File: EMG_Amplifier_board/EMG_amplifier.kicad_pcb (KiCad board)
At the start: 2 copper layers, 50 x 28 mm, 54 parts, among them J1 Conn_01x04_Socket, J2 Conn_01x04_Pin, J3 Conn_01x06_Pin, J4 Conn_01x06_Socket, J7 Conn_01x06_Pin, U1 LPV821DBVR, U2 INA333xxDGK, U3 LPV821DBVR, U5 LPV821DBVR, U6 LPV821DBVR, U7 TPD2E001DRLR, U8 TLV8542DR

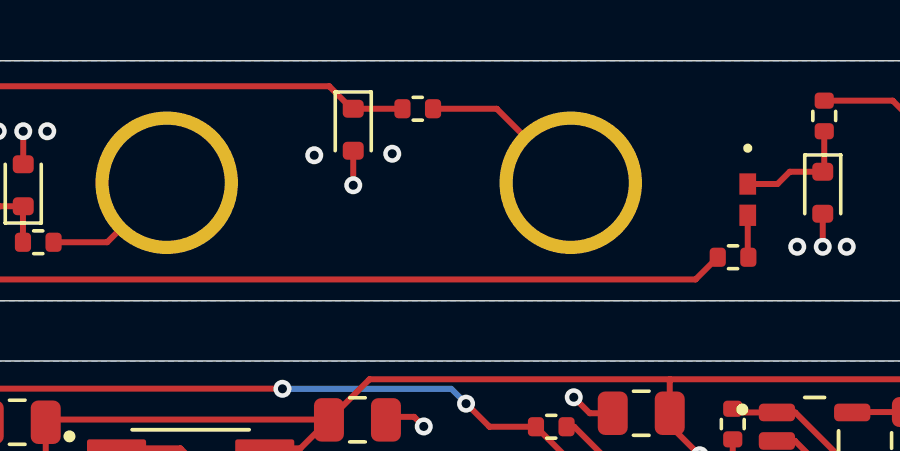
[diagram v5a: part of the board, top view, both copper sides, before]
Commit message: update R and C refs to correspond to paper
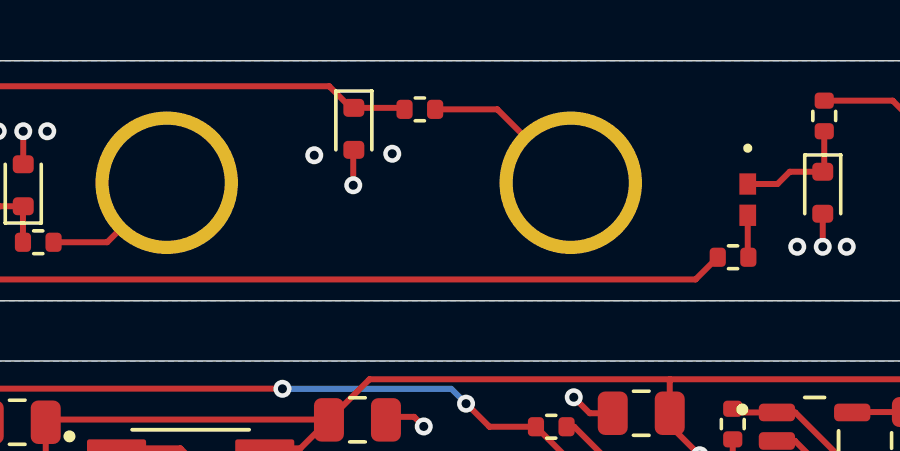
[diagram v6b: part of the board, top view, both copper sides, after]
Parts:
- moved R5 0.07 mm to (35.0, 13.6)
- renumbered C4 to C10, C7 to C20, C9 to C21, C8 to C22, C11 to C23, C10 to C24, C5 to C3, C6 to C4, C3 to C9, R20 to R10, R19 to R11, R14 to R12, R12 to R13, R13 to R14, R10 to R22, R11 to R23, R23 to R31, R24 to R32, R21 to R33, R22 to R34
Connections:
- C9 pad 1: Net-(U1-IN+) -> GND
- C9 pad 2: GND -> Net-(U1-IN+)
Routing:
- net Net-(U1-IN+): track 3.30 -> 4.14 mm, vias 0 -> 1
- net GND: track 40.1 -> 39.3 mm, vias 41 -> 40

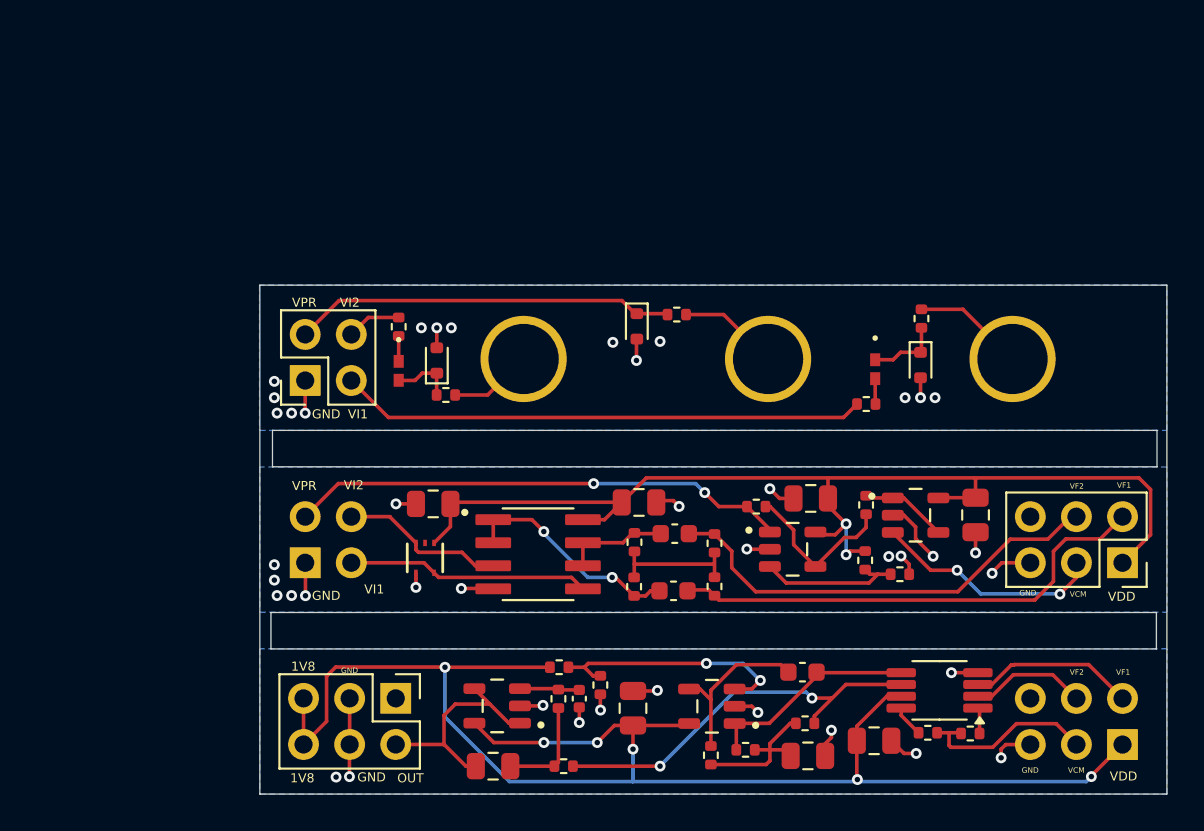
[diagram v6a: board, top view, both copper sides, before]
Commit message: replace 2012 capacitors with 1005
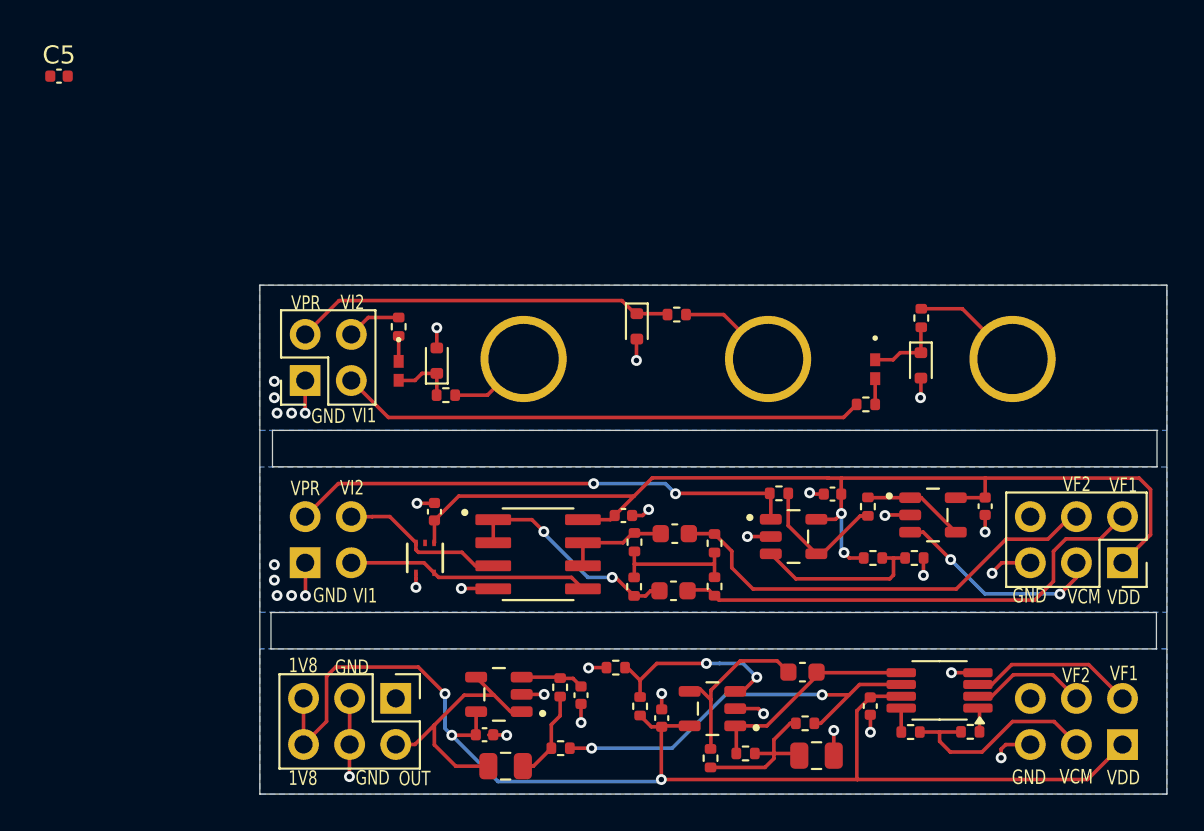
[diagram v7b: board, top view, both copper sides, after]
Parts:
- added C25: 0.1uF, Capacitor_SMD:C_0402_1005Metric, F.Cu at (45.6, 35.2)
- added C5: 0.1uF, Capacitor_SMD:C_0402_1005Metric, F.Cu at (0.94, 0.48)
- C12, C20, C21, C22, C23, C24: footprint Capacitor_SMD:C_0805_2012Metric -> Capacitor_SMD:C_0402_1005Metric
- moved C24 11.8 mm to (34.1, 35.9), turned to 90 degrees
- moved C23 8.31 mm to (24.4, 36.8), turned to 0 degrees
- moved R33 4.95 mm to (33.0, 35.2), turned to 90 degrees
- moved R16 1.45 mm to (40.6, 23.5)
- moved R34 1.28 mm to (31.6, 33.1), turned to 180 degrees
- moved C21 1.22 mm to (43.5, 23.5)
- moved R32 1.20 mm to (48.1, 27.0)
- moved C20 1.12 mm to (32.0, 24.7)
- moved R22 1.00 mm to (28.6, 37.5)
- moved U5 0.96 mm to (49.1, 24.7)
- moved R14 0.95 mm to (47.9, 36.6)
- moved C22 0.71 mm to (52.0, 24.2)
- moved U6 0.70 mm to (41.4, 25.9)
- moved C10 0.69 mm to (25.5, 38.5)
- moved R23 0.64 mm to (28.5, 34.2)
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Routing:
- net +1V8: track 83.8 -> 71.0 mm, vias 6 -> 3
- net Net-(U3-IN+): track 13.7 -> 10.8 mm
- net GND: track 39.3 -> 36.4 mm, vias 40 -> 34
- net /Processing_Board/V_EMG_OUT: track 12.6 -> 14.4 mm
- net Net-(U6-IN+): track 7.83 -> 9.62 mm
- net /Processing_Board/V_CM: track 10.2 -> 11.8 mm
- net Net-(U6-IN-): track 9.18 -> 7.78 mm
- net /Filtering_Board/V_CM: track 12.8 -> 11.8 mm
- net Net-(U5-IN-): track 4.82 -> 5.64 mm
- net Net-(C10-Pad1): track 5.76 -> 5.03 mm
- net Net-(U1-IN+): track 4.14 -> 3.45 mm, vias 1 -> 0
- net Net-(C4-Pad1): track 8.31 -> 8.82 mm

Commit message: minor changes
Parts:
- removed C5: 0.1uF, Capacitor_SMD:C_0402_1005Metric
- U1, U3, U5, U6: footprint Components:SOT95P280X145-5N -> LPV821DBVR:SOT95P280X145-5N
- moved C12 0.87 mm to (21.1, 25.2), turned to 0 degrees
- moved C3 0.45 mm to (41.4, 33.3)
- moved R13 0.36 mm to (50.8, 36.6)
- moved R14 0.36 mm to (47.5, 36.6)
- moved U2 0.36 mm to (49.1, 34.3)
- moved C22 0.27 mm to (51.7, 24.2)
- moved R11 0.26 mm to (38.7, 37.5)
- moved C25 0.25 mm to (45.4, 35.1)
- moved R16 0.20 mm to (40.6, 23.7)
- moved C24 0.19 mm to (34.3, 35.8)
- moved C21 0.15 mm to (43.5, 23.7)
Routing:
- net +1V8: track 71.0 -> 66.3 mm
- net GND: track 36.4 -> 34.5 mm, vias 34 -> 33
